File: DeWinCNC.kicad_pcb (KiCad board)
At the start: 2 copper layers, 99.7 x 99.3 mm, 87 parts, among them J1 Digital, J10 Vcc, J11 S3, J12 Aux-1a, J13 S4, J14 X-axis, J15 Y-axis, J16 Z-axis, J18 A-axis, J19 X-, J2 Aux-4, J20 X+, J21 Y-, J22 Y+, J23 Z-, J24 Z+, J25 B-axis, J261 RLA2, J262 RLA3, J27 T1 T2 T3, J28 RLA1, J29 I2C, J3 S1, J30 RLA4, J31 0V / 5V, J32 0V / 5V, J33 0V / 5V, J34 0V / 5V, J35 0V / 5V, J36 PWM, J37 1-Wire, J38 IDC for DB37, J39 D7, J4 Vcc, J40 Limits, J41 Limit, J42 Limit, J43 Limit, J44 Limit, J45 Limit, J46 Limit, J47 1-Wire, J5 5v,PS_ON,Vcc, J6 Aux-1b, J7 S2, J8 Aux-2, J9 Aux-3, P10 CONN_01X01, P11 CONN_01X01, U1 S102S01, U2 S102S01, U3 S102S01, U4 S102S01, U5 LM7812_TO220

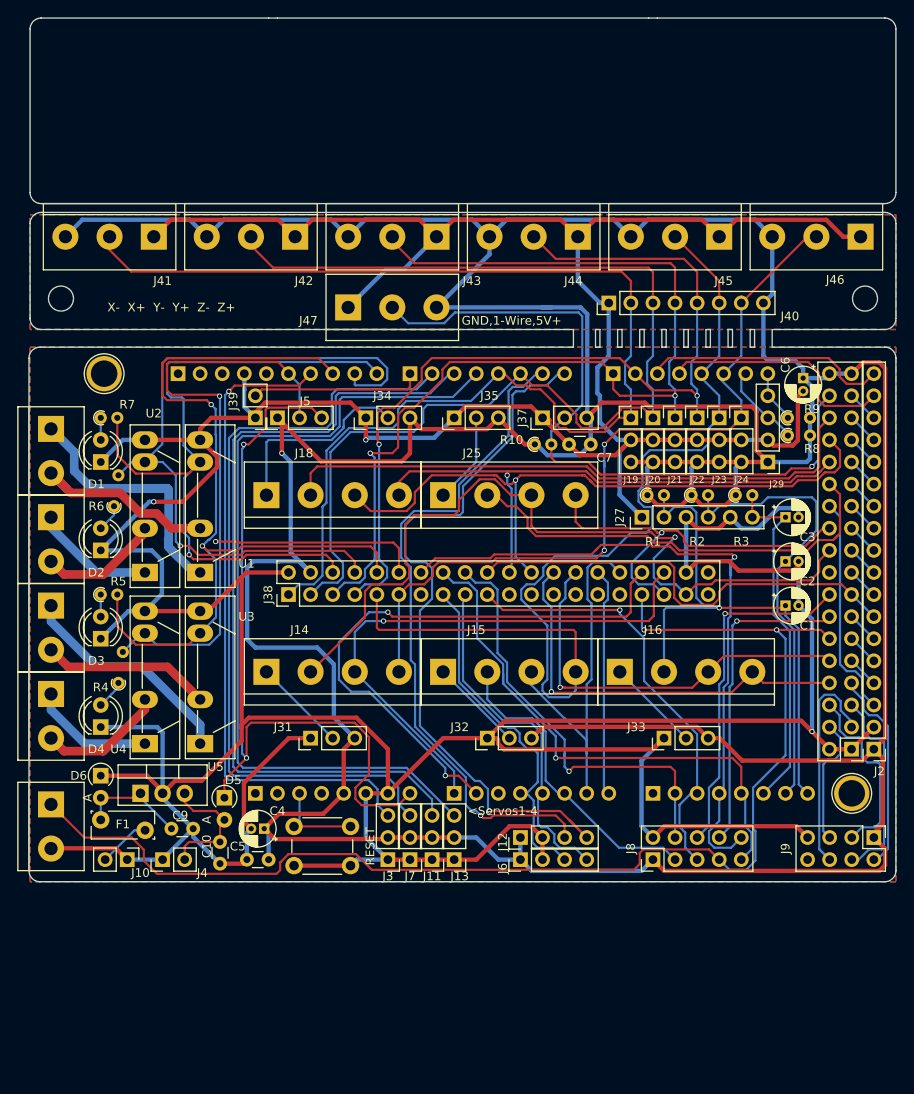
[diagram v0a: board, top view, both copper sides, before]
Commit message: Update ESP pinout, round edges more.
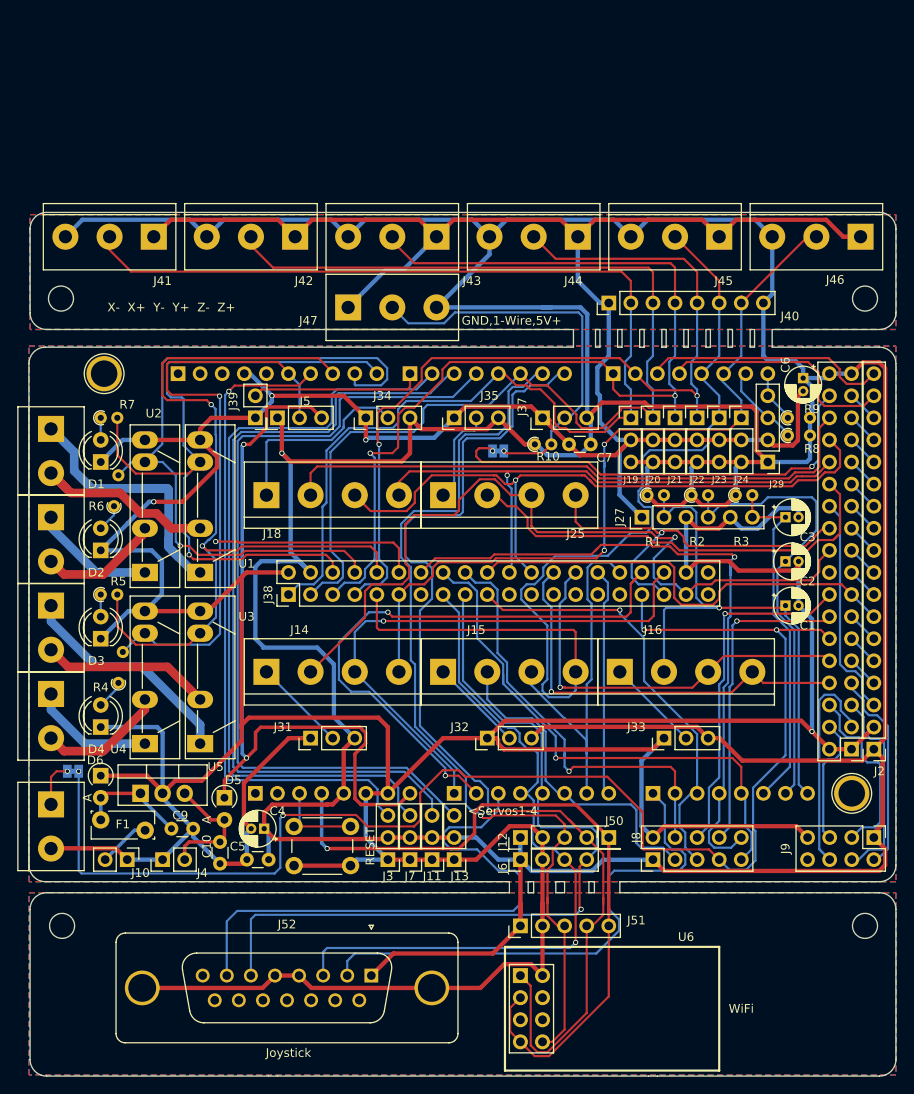
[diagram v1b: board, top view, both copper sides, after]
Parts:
- added J50: 3.3v, Connector_PinHeader_2.54mm:PinHeader_1x01_P2.54mm_Vertical, F.Cu at (177.8, 124.5)
- added J51: Serial0, Connector_PinHeader_2.54mm:PinHeader_1x05_P2.54mm_Vertical, F.Cu at (167.6, 134.6)
- added J52: DB15_Joystick, Connector_Dsub:DSUB-15_Female_Vertical_P2.77x2.84mm_MountingHoles, F.Cu at (150.5, 140.3)
- added JP48: D56,D57,D62?, Jumper:SolderJumper-2_P1.3mm_Bridged_Pad1.0x1.5mm, B.Cu at (165.1, 80.0)
- added JP49: Laser/Spindle, Jumper:SolderJumper-2_P1.3mm_Bridged_Pad1.0x1.5mm, B.Cu at (116.2, 116.8)
- added U6: ESP-01v090, ESP8266:ESP-01, F.Cu at (167.6, 140.3)
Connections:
- J36 pad 1: /D44 -> Net-(J36-Pad1)
- J37 pad 2: /D22 -> Net-(J37-Pad2)
- J47 pad 2: /D22 -> Net-(J37-Pad2)
- JM5 pad 4: Net-(JM5-Pad4) -> /3.3v
- R10 pad 2: /D22 -> Net-(J37-Pad2)
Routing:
- net /3.3v: track 0.00 -> 82.7 mm, vias 0 -> 1
- net GND: track 653.3 -> 718.2 mm, vias 3 -> 4
- net /D56(A2): track 0.00 -> 64.8 mm
- net /D62(A8): track 0.00 -> 60.8 mm
- net /D58(A4): track 40.6 -> 95.6 mm, vias 0 -> 1
- net Net-(J37-Pad2): track 0.00 -> 45.8 mm, vias 0 -> 1
- net /D57(A3): track 40.3 -> 82.5 mm, vias 0 -> 1
- net /D0(Rx0): track 85.6 -> 127.8 mm
- net /D1(Tx0): track 79.5 -> 109.7 mm
- net /D22: track 82.0 -> 52.5 mm, vias 1 -> 2
- net +5V: track 549.7 -> 575.2 mm
- net /D44: track 144.9 -> 162.8 mm, vias 2 -> 4
- net Net-(J36-Pad1): track 0.00 -> 5.31 mm, vias 0 -> 1
- net /D59(A5): track 35.7 -> 37.9 mm
- net /Vcc: track 87.8 -> 86.3 mm
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- removed copper zone on B.Cu, net +5V
- removed copper zone on F.Cu, net +5V
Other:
- outline, holes or cut-outs redrawn
- net class LowPower added: clearance 0.2, trace_width 0.4, via_dia 0.6, via_drill 0.4
- board text added: "DEWINCNC (c)2020 TechColab"
- board text added: "Joystick"
- board text added: "Rev 0.12"
- board text added: "WiFi"
- board text removed: "DeWinCNC (c)2020 TechColab"
- board text removed: "Rev 0.9"
